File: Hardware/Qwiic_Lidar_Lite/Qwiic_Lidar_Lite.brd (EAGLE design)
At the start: 13.7 x 23 mm, 21 parts, among them U1 XC9140

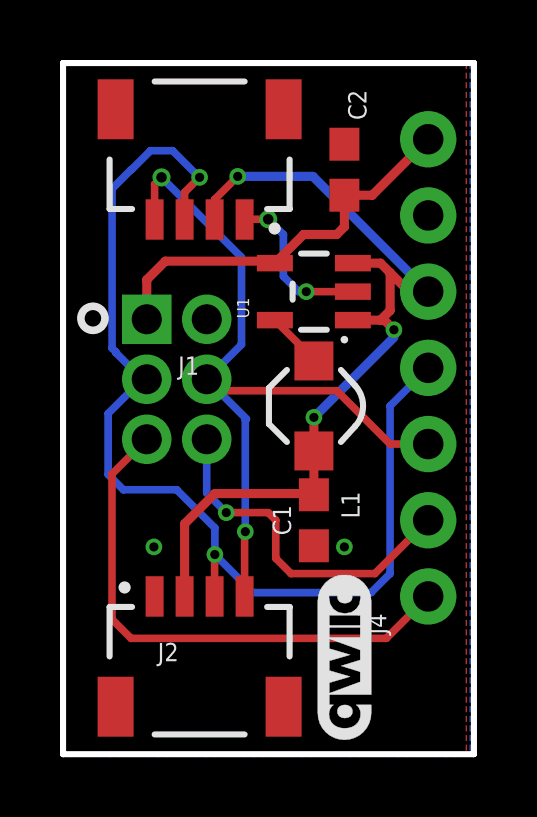
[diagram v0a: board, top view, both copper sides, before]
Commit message: Updated board design with power LED
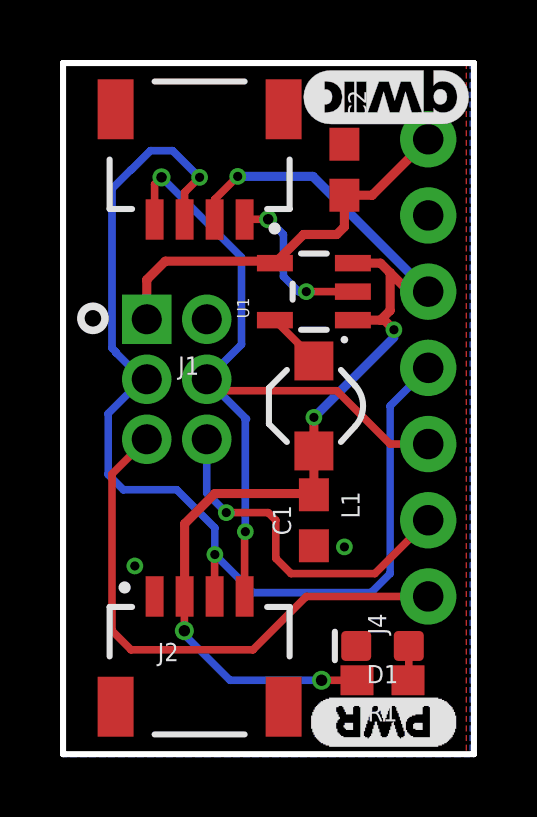
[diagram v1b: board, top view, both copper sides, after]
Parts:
- added D1: RED, SparkFun-LED:LED-0603
- added R1: 1k, SparkFun-Resistors:0603
- added U$12: (no value), buzzard_labels (6):PWR0
- moved LOGO1 18.7 mm to (11.3, 23.0), turned to 180 degrees
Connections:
- new net N$1: D1.A, R1.1
- net 3.3V: now also R1.2
- net GND: now also D1.C
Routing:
- net 3.3V: track 29.6 -> 37.2 mm, vias 3 -> 5
- net N$1: track 0.00 -> 1.15 mm
- net GPIOA: track 17.9 -> 18.4 mm
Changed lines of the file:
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@@
 <element name="U$1" library="buzzard_labels (2)" package="GND3" value="" x="7.62" y="19.05" smashed="yes" rot="MR180"/>
 <element name="U$2" library="buzzard_labels (2)" package="3V30" value="" x="7.747" y="16.51" smashed="yes" rot="MR180"/>
-<element name="LOGO1" library="SparkFun-Aesthetics" package="QWIIC_5.5MM" value="QWIIC_LOGO_CONNECTOR" x="9.906" y="4.318" smashed="yes" rot="R90"/>
+<element name="LOGO1" library="SparkFun-Aesthetics" package="QWIIC_5.5MM" value="QWIIC_LOGO_CONNECTOR" x="11.303" y="22.987" smashed="yes" rot="R180"/>
 <element name="U$8" library="SparkX" package="SPARKX-MEDIUM" value="SPARKX-LOGO4" x="9.017" y="2.921" smashed="yes" rot="MR180"/>
 <element name="J4" library="SparkFun-Connectors" package="1X07_NO_SILK" value="" x="12.7" y="6.35" smashed="yes" rot="R90">
@@
 <element name="U$9" library="buzzard_labels (5)" package="QWIIC0" value="" x="0" y="21.082" smashed="yes" rot="MR180"/>
 <element name="U$11" library="buzzard_labels (5)" package="LIDAR#LITE1" value="" x="0" y="22.86" smashed="yes" rot="MR180"/>
+<element name="D1" library="SparkFun-LED" package="LED-0603" value="RED" x="11.176" y="4.699" smashed="yes" rot="R180">
+<attribute name="NAME" x="11.176" y="4.064" size="0.6096" layer="25" font="vector" ratio="20" rot="R180" align="bottom-center"/>
+<attribute name="PROD_ID" value="DIO-00819" x="11.176" y="4.699" size="1.778" layer="27" ratio="15" rot="R180" display="off"/>
+<attribute name="VALUE" x="11.176" y="5.334" size="0.6096" layer="27" font="vector" ratio="20" rot="R180" align="top-center"/>
+</element>
+<element name="R1" library="SparkFun-Resistors" package="0603" value="1k" x="11.176" y="3.556" smashed="yes" rot="R180">
+<attribute name="NAME" x="11.176" y="2.794" size="0.6096" layer="25" font="vector" ratio="20" rot="R180" align="bottom-center"/>
+<attribute name="PROD_ID" value="RES-07856" x="11.176" y="3.556" size="1.778" layer="27" ratio="15" rot="R180" display="off"/>
+<attribute name="VALUE" x="11.176" y="4.318" size="0.6096" layer="27" font="vector" ratio="20" rot="R180" align="top-center"/>
+</element>
+<element name="U$12" library="buzzard_labels (6)" package="PWR0" value="" x="13.716" y="2.159" smashed="yes" rot="R180"/>
 </elements>
 <signals>
@@
 <contactref element="J3" pad="5"/>
 <contactref element="J4" pad="1"/>
-<wire x1="12.7" y1="6.35" x2="11.303" y2="4.953" width="0.254" layer="1"/>
-<wire x1="11.303" y1="4.953" x2="2.794" y2="4.953" width="0.254" layer="1"/>
-<wire x1="2.794" y1="4.953" x2="2.159" y2="5.588" width="0.254" layer="1"/>
 <wire x1="2.159" y1="10.43" x2="3.318" y2="11.589" width="0.254" layer="1"/>
-<wire x1="2.159" y1="5.588" x2="2.159" y2="10.43" width="0.254" layer="1"/>
+<wire x1="6.858" y1="4.572" x2="2.794" y2="4.572" width="0.254" layer="1"/>
+<wire x1="12.7" y1="6.35" x2="8.636" y2="6.35" width="0.254" layer="1"/>
+<wire x1="8.636" y1="6.35" x2="6.858" y2="4.572" width="0.254" layer="1"/>
+<wire x1="2.794" y1="4.572" x2="2.159" y2="5.207" width="0.254" layer="1"/>
+<wire x1="2.159" y1="5.207" x2="2.159" y2="10.43" width="0.254" layer="1"/>
 </signal>
 <signal name="GND">
@@
 <contactref element="J4" pad="6"/>
 <via x="9.906" y="8.001" extent="1-16" drill="0.3048"/>
-<via x="3.556" y="8.001" extent="1-16" drill="0.3048"/>
+<via x="2.921" y="7.366" extent="1-16" drill="0.3048"/>
 <wire x1="6.58" y1="18.915" x2="6.588" y2="18.923" width="0.254" layer="1"/>
 <wire x1="6.588" y1="18.923" x2="7.366" y2="18.923" width="0.254" layer="1"/>
@@
 <wire x1="7.874" y1="17.018" x2="8.382" y2="16.51" width="0.254" layer="16"/>
 <wire x1="8.382" y1="16.51" x2="8.636" y2="16.51" width="0.254" layer="16"/>
+<contactref element="D1" pad="C"/>
 </signal>
 <signal name="SCL">
@@
 <wire x1="5.58" y1="18.915" x2="5.58" y2="19.582" width="0.254" layer="1"/>
 <wire x1="5.58" y1="19.582" x2="6.35" y2="20.352" width="0.254" layer="1"/>
+<contactref element="R1" pad="2"/>
+<wire x1="4.572" y1="6.342" x2="4.58" y2="6.35" width="0.254" layer="1"/>
+<via x="9.144" y="3.556" extent="1-16" drill="0.381"/>
+<wire x1="9.144" y1="3.556" x2="6.096" y2="3.556" width="0.254" layer="16"/>
+<wire x1="6.096" y1="3.556" x2="4.572" y2="5.08" width="0.254" layer="16"/>
+<wire x1="4.572" y1="5.08" x2="4.572" y2="5.207" width="0.254" layer="16"/>
+<via x="4.572" y="5.207" extent="1-16" drill="0.381"/>
+<wire x1="4.572" y1="5.207" x2="4.572" y2="6.342" width="0.254" layer="1"/>
+<wire x1="10.326" y1="3.556" x2="9.144" y2="3.556" width="0.254" layer="1"/>
 </signal>
 <signal name="N$2">
@@
 <wire x1="10.834" y1="19.724" x2="9.906" y2="19.724" width="0.3048" layer="1"/>
 </signal>
+<signal name="N$1">
+<contactref element="D1" pad="A"/>
+<contactref element="R1" pad="1"/>
+<wire x1="12.026" y1="3.556" x2="12.053" y2="3.583" width="0.254" layer="1"/>
+<wire x1="12.053" y1="3.583" x2="12.053" y2="4.699" width="0.254" layer="1"/>
+</signal>
 </signals>

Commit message: Stuff and things
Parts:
- added LOGO2: OSHW-LOGOMINI, SparkFun-Aesthetics:OSHW-LOGO-MINI
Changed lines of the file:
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@@
 <layers>
 <layer number="1" name="Top" color="4" fill="1" visible="yes" active="yes"/>
-<layer number="2" name="Route2" color="16" fill="1" visible="no" active="no"/>
-<layer number="15" name="Route15" color="23" fill="1" visible="no" active="no"/>
 <layer number="16" name="Bottom" color="1" fill="1" visible="yes" active="yes"/>
 <layer number="17" name="Pads" color="2" fill="1" visible="yes" active="yes"/>
@@
 <layer number="23" name="tOrigins" color="15" fill="1" visible="yes" active="yes"/>
 <layer number="24" name="bOrigins" color="15" fill="1" visible="yes" active="yes"/>
-<layer number="25" name="tNames" color="7" fill="1" visible="yes" active="yes"/>
-<layer number="26" name="bNames" color="7" fill="1" visible="yes" active="yes"/>
-<layer number="27" name="tValues" color="7" fill="1" visible="yes" active="yes"/>
-<layer number="28" name="bValues" color="7" fill="1" visible="yes" active="yes"/>
-<layer number="29" name="tStop" color="7" fill="3" visible="yes" active="yes"/>
-<layer number="30" name="bStop" color="7" fill="6" visible="yes" active="yes"/>
-<layer number="31" name="tCream" color="7" fill="4" visible="yes" active="yes"/>
-<layer number="32" name="bCream" color="7" fill="5" visible="yes" active="yes"/>
-<layer number="33" name="tFinish" color="6" fill="3" visible="yes" active="yes"/>
-<layer number="34" name="bFinish" color="6" fill="6" visible="yes" active="yes"/>
-<layer number="35" name="tGlue" color="7" fill="4" visible="yes" active="yes"/>
-<layer number="36" name="bGlue" color="7" fill="5" visible="yes" active="yes"/>
-<layer number="37" name="tTest" color="7" fill="1" visible="yes" active="yes"/>
-<layer number="38" name="bTest" color="7" fill="1" visible="yes" active="yes"/>
-<layer number="39" name="tKeepout" color="4" fill="11" visible="yes" active="yes"/>
-<layer number="40" name="bKeepout" color="1" fill="11" visible="yes" active="yes"/>
-<layer number="41" name="tRestrict" color="4" fill="10" visible="yes" active="yes"/>
-<layer number="42" name="bRestrict" color="1" fill="10" visible="yes" active="yes"/>
-<layer number="43" name="vRestrict" color="2" fill="10" visible="yes" active="yes"/>
-<layer number="44" name="Drills" color="7" fill="1" visible="yes" active="yes"/>
+<layer number="25" name="tNames" color="7" fill="1" visible="no" active="yes"/>
+<layer number="26" name="bNames" color="7" fill="1" visible="no" active="yes"/>
+<layer number="27" name="tValues" color="7" fill="1" visible="no" active="yes"/>
+<layer number="28" name="bValues" color="7" fill="1" visible="no" active="yes"/>
+<layer number="29" name="tStop" color="7" fill="3" visible="no" active="yes"/>
+<layer number="30" name="bStop" color="7" fill="6" visible="no" active="yes"/>
+<layer number="31" name="tCream" color="7" fill="4" visible="no" active="yes"/>
+<layer number="32" name="bCream" color="7" fill="5" visible="no" active="yes"/>
+<layer number="33" name="tFinish" color="6" fill="3" visible="no" active="yes"/>
+<layer number="34" name="bFinish" color="6" fill="6" visible="no" active="yes"/>
+<layer number="35" name="tGlue" color="7" fill="4" visible="no" active="yes"/>
+<layer number="36" name="bGlue" color="7" fill="5" visible="no" active="yes"/>
+<layer number="37" name="tTest" color="7" fill="1" visible="no" active="yes"/>
+<layer number="38" name="bTest" color="7" fill="1" visible="no" active="yes"/>
+<layer number="39" name="tKeepout" color="4" fill="11" visible="no" active="yes"/>
+<layer number="40" name="bKeepout" color="1" fill="11" visible="no" active="yes"/>
+<layer number="41" name="tRestrict" color="4" fill="10" visible="no" active="yes"/>
+<layer number="42" name="bRestrict" color="1" fill="10" visible="no" active="yes"/>
+<layer number="43" name="vRestrict" color="2" fill="10" visible="no" active="yes"/>
+<layer number="44" name="Drills" color="7" fill="1" visible="no" active="yes"/>
 <layer number="45" name="Holes" color="7" fill="1" visible="yes" active="yes"/>
 <layer number="46" name="Milling" color="3" fill="1" visible="yes" active="yes"/>
-<layer number="47" name="Measures" color="7" fill="1" visible="yes" active="yes"/>
-<layer number="48" name="Document" color="7" fill="1" visible="yes" active="yes"/>
-<layer number="49" name="Reference" color="7" fill="1" visible="yes" active="yes"/>
-<layer number="50" name="dxf" color="7" fill="1" visible="no" active="no"/>
-<layer number="51" name="tDocu" color="5" fill="1" visible="yes" active="yes"/>
-<layer number="52" name="bDocu" color="7" fill="1" visible="yes" active="yes"/>
+<layer number="47" name="Measures" color="7" fill="1" visible="no" active="yes"/>
+<layer number="48" name="Document" color="7" fill="1" visible="no" active="yes"/>
+<layer number="49" name="Reference" color="7" fill="1" visible="no" active="yes"/>
+<layer number="50" name="dxf" color="7" fill="1" visible="no" active="yes"/>
+<layer number="51" name="tDocu" color="6" fill="1" visible="yes" active="yes"/>
+<layer number="52" name="bDocu" color="7" fill="1" visible="no" active="yes"/>
+<layer number="91" name="Nets" color="2" fill="1" visible="no" active="no"/>
+<layer number="92" name="Busses" color="1" fill="1" visible="no" active="no"/>
+<layer number="93" name="Pins" color="2" fill="1" visible="no" active="no"/>
+<layer number="94" name="Symbols" color="4" fill="1" visible="no" active="no"/>
+<layer number="95" name="Names" color="7" fill="1" visible="no" active="no"/>
+<layer number="96" name="Values" color="7" fill="1" visible="no" active="no"/>
+<layer number="2" name="Route2" color="16" fill="1" visible="no" active="no"/>
+<layer number="15" name="Route15" color="23" fill="1" visible="no" active="no"/>
 <layer number="53" name="tGND_GNDA" color="7" fill="9" visible="no" active="no"/>
 <layer number="54" name="bGND_GNDA" color="1" fill="9" visible="no" active="no"/>
@@
 <layer number="89" name="SimProbes" color="9" fill="1" visible="no" active="no"/>
 <layer number="90" name="Modules" color="5" fill="1" visible="no" active="no"/>
-<layer number="91" name="Nets" color="2" fill="1" visible="no" active="no"/>
-<layer number="92" name="Busses" color="1" fill="1" visible="no" active="no"/>
-<layer number="93" name="Pins" color="2" fill="1" visible="no" active="no"/>
-<layer number="94" name="Symbols" color="4" fill="1" visible="no" active="no"/>
-<layer number="95" name="Names" color="7" fill="1" visible="no" active="no"/>
-<layer number="96" name="Values" color="7" fill="1" visible="no" active="no"/>
 <layer number="97" name="Info" color="7" fill="1" visible="no" active="no"/>
 <layer number="98" name="Guide" color="6" fill="1" visible="no" active="no"/>
@@
 <layer number="115" name="ReferenceISLANDS" color="7" fill="1" visible="no" active="no"/>
 <layer number="116" name="Patch_BOT" color="9" fill="4" visible="no" active="no"/>
-<layer number="117" name="PM_Ref" color="26" fill="1" visible="yes" active="yes"/>
+<layer number="117" name="PM_Ref" color="26" fill="1" visible="no" active="no"/>
 <layer number="118" name="Rect_Pads" color="7" fill="1" visible="no" active="no"/>
-<layer number="119" name="PF_Ref" color="31" fill="1" visible="yes" active="yes"/>
-<layer number="120" name="WFL_Ref" color="25" fill="1" visible="yes" active="yes"/>
+<layer number="119" name="PF_Ref" color="31" fill="1" visible="no" active="no"/>
+<layer number="120" name="WFL_Ref" color="25" fill="1" visible="no" active="no"/>
 <layer number="121" name="_tsilk" color="7" fill="1" visible="no" active="no"/>
 <layer number="122" name="_bsilk" color="7" fill="1" visible="no" active="no"/>
@@
 </element>
 <element name="U$12" library="buzzard_labels (6)" package="PWR0" value="" x="13.716" y="2.159" smashed="yes" rot="R180"/>
+<element name="LOGO2" library="SparkFun-Aesthetics" package="OSHW-LOGO-MINI" value="OSHW-LOGOMINI" x="2.413" y="3.048" smashed="yes" rot="MR180"/>
 </elements>
 <signals>
